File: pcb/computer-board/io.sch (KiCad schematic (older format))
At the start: 17 parts, among them J4 Conn_02x20_Odd_Even, U5 SN74AVC16T245DGGR, U6 SN74AVC4T245PWR, U7 74LVC1G14GW,125

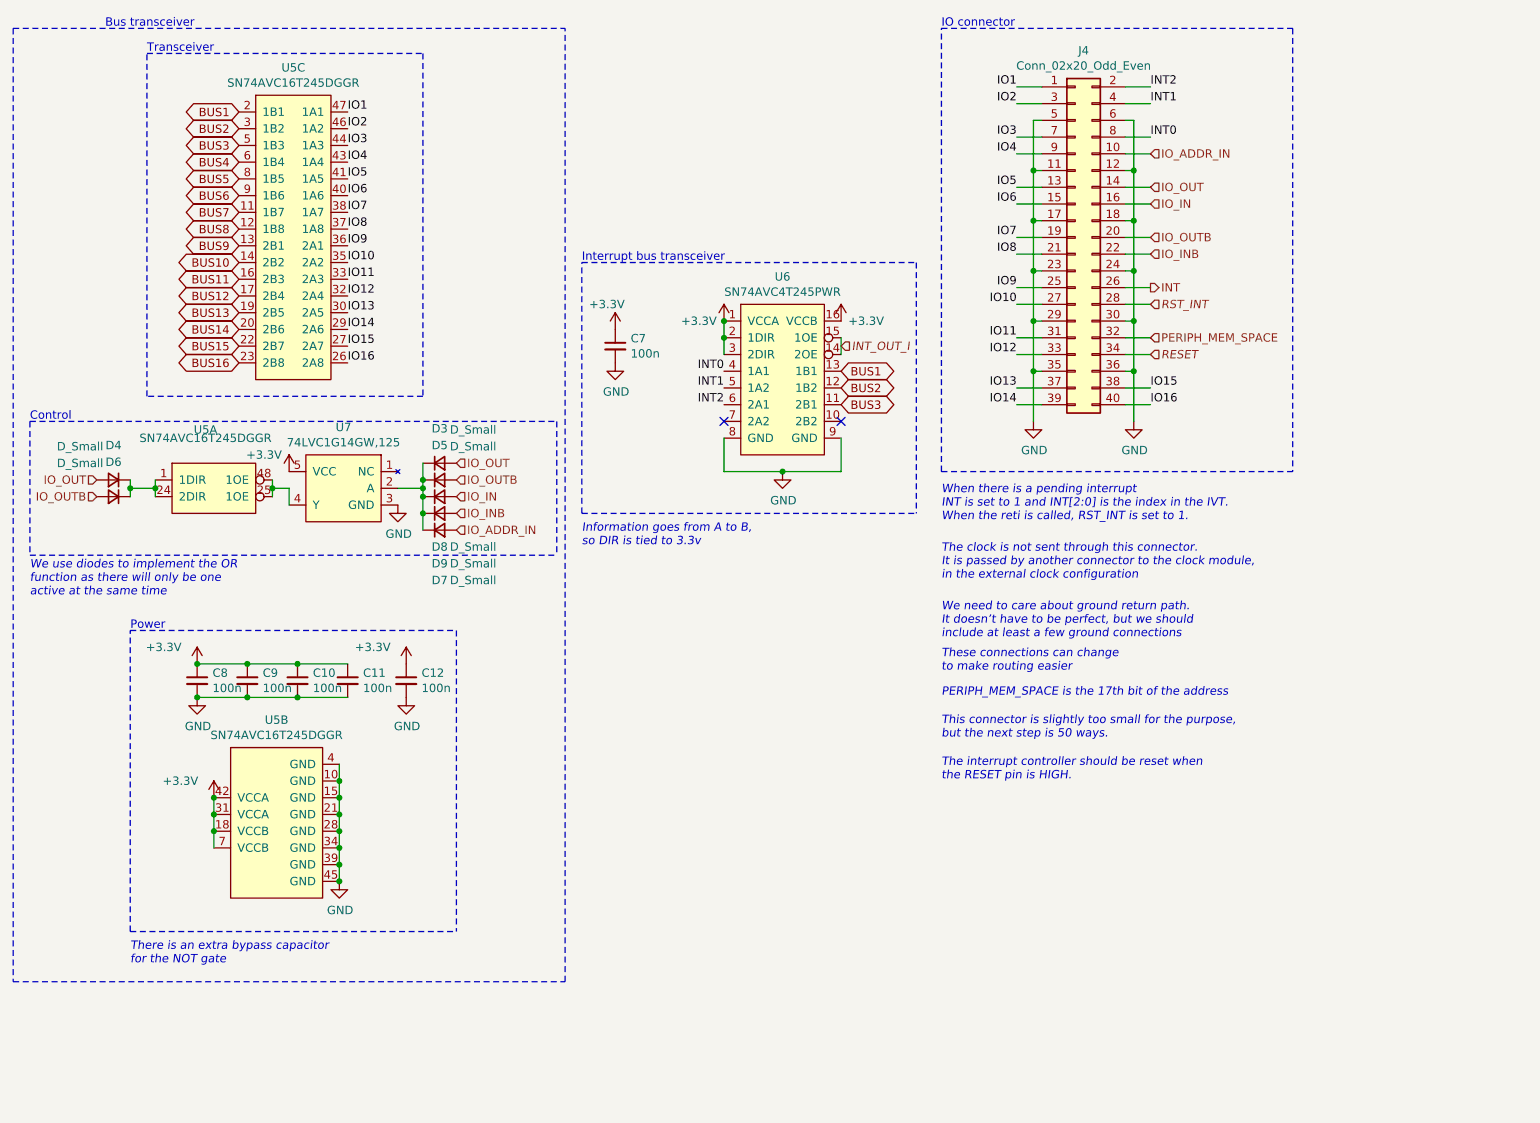
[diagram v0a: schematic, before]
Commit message: Remove and change connectors for a mezzanine one
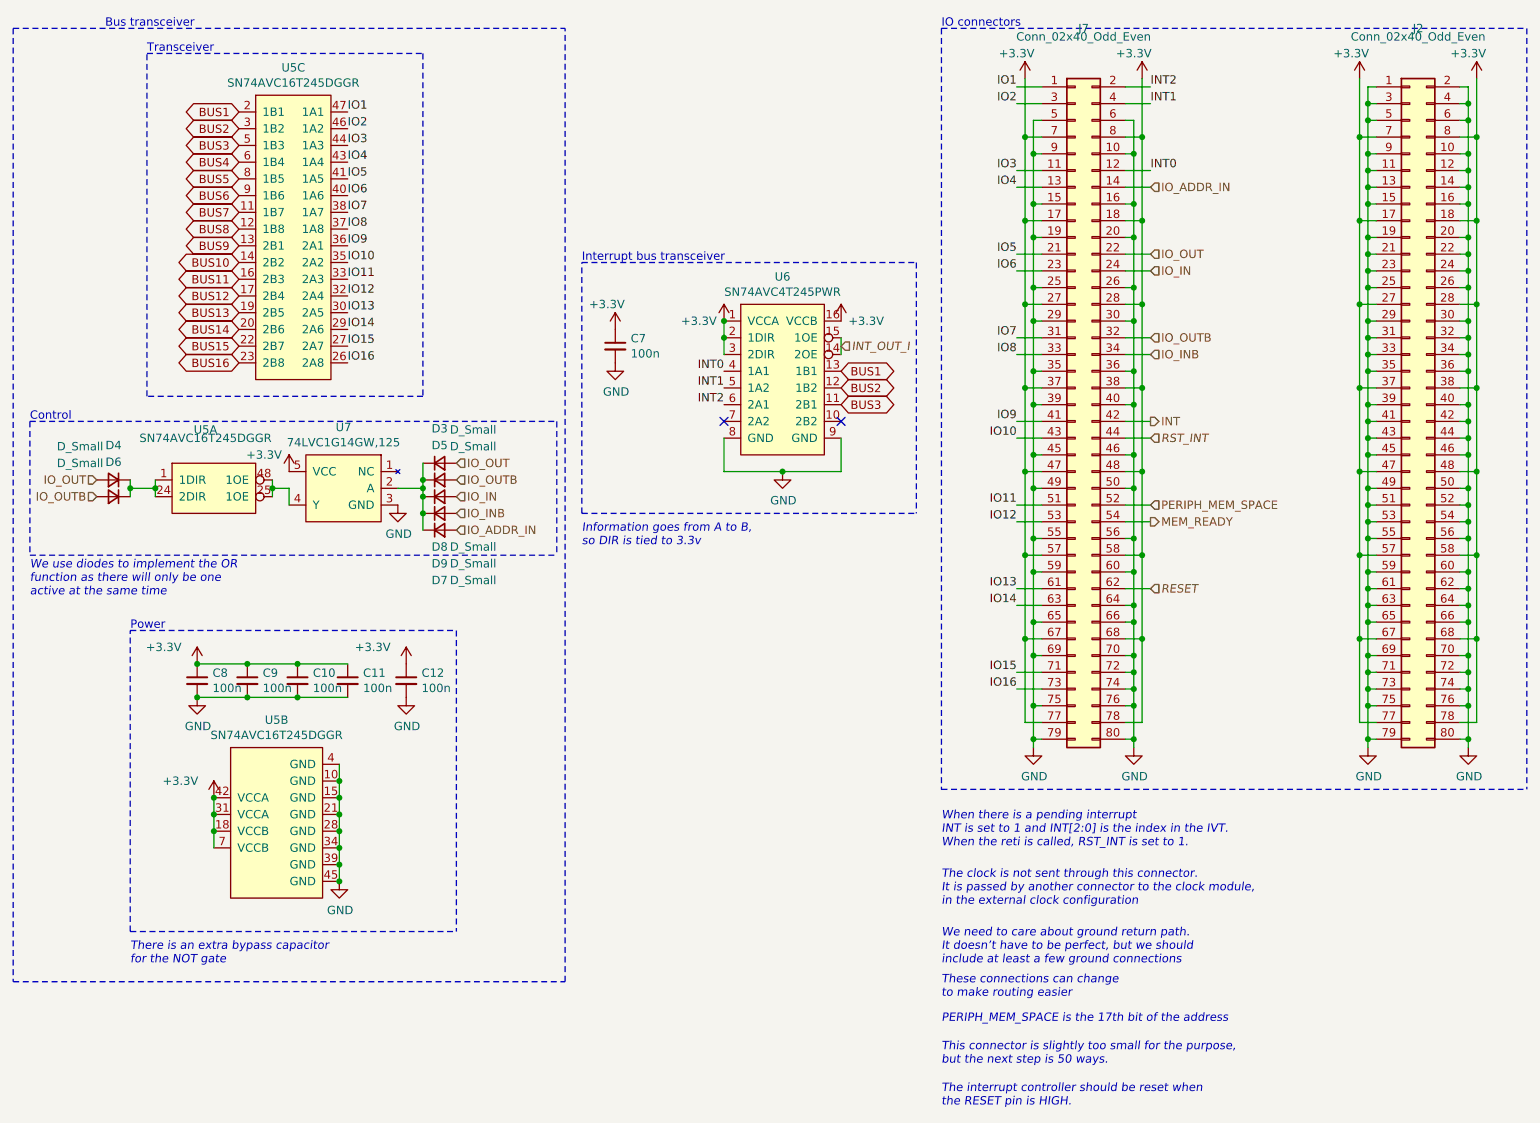
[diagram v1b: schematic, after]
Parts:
- removed J4: Conn_02x20_Odd_Even, Connector_Molex:Micro-Lock-Plus-02x20, symbol Connector_Generic:Conn_02x20_Odd_Even
- added J2, J7: Conn_02x40_Odd_Even, Connector_Hirose:HRS_DF17(2.0)-80DP-0.5V(57), symbol Connector_Generic:Conn_02x40_Odd_Even
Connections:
- net +3V3: now also J2.17 (Pin_17), J2.18 (Pin_18), J2.27 (Pin_27), J2.28 (Pin_28), J2.37 (Pin_37), J2.38 (Pin_38), J2.47 (Pin_47), J2.48 (Pin_48), J2.57 (Pin_57), J2.58 (Pin_58), J2.67 (Pin_67), J2.68 (Pin_68), J2.7 (Pin_7), J2.77 (Pin_77), J2.78 (Pin_78), J2.8 (Pin_8), J7.17 (Pin_17), J7.18 (Pin_18), J7.27 (Pin_27), J7.28 (Pin_28), J7.37 (Pin_37), J7.38 (Pin_38), J7.47 (Pin_47), J7.48 (Pin_48), J7.57 (Pin_57), J7.58 (Pin_58), J7.67 (Pin_67), J7.68 (Pin_68), J7.7 (Pin_7), J7.77 (Pin_77), J7.78 (Pin_78), J7.8 (Pin_8)
- net GND: now also J2.1 (Pin_1), J2.10 (Pin_10), J2.11 (Pin_11), J2.12 (Pin_12), J2.13 (Pin_13), J2.14 (Pin_14), J2.15 (Pin_15), J2.16 (Pin_16), J2.19 (Pin_19), J2.2 (Pin_2), J2.20 (Pin_20), J2.21 (Pin_21), J2.22 (Pin_22), J2.23 (Pin_23), J2.24 (Pin_24), J2.25 (Pin_25), J2.26 (Pin_26), J2.29 (Pin_29), J2.3 (Pin_3), J2.30 (Pin_30), J2.31 (Pin_31), J2.32 (Pin_32), J2.33 (Pin_33), J2.34 (Pin_34), J2.35 (Pin_35), J2.36 (Pin_36), J2.39 (Pin_39), J2.4 (Pin_4), J2.40 (Pin_40), J2.41 (Pin_41), J2.42 (Pin_42), J2.43 (Pin_43), J2.44 (Pin_44), J2.45 (Pin_45), J2.46 (Pin_46), J2.49 (Pin_49), J2.5 (Pin_5), J2.50 (Pin_50), J2.51 (Pin_51), J2.52 (Pin_52), J2.53 (Pin_53), J2.54 (Pin_54), J2.55 (Pin_55), J2.56 (Pin_56), J2.59 (Pin_59), J2.6 (Pin_6), J2.60 (Pin_60), J2.61 (Pin_61), J2.62 (Pin_62), J2.63 (Pin_63), J2.64 (Pin_64), J2.65 (Pin_65), J2.66 (Pin_66), J2.69 (Pin_69), J2.70 (Pin_70), J2.71 (Pin_71), J2.72 (Pin_72), J2.73 (Pin_73), J2.74 (Pin_74), J2.75 (Pin_75), J2.76 (Pin_76), J2.79 (Pin_79), J2.80 (Pin_80), J2.9 (Pin_9), J7.10 (Pin_10), J7.15 (Pin_15), J7.16 (Pin_16), J7.19 (Pin_19), J7.20 (Pin_20), J7.25 (Pin_25), J7.26 (Pin_26), J7.29 (Pin_29), J7.30 (Pin_30), J7.35 (Pin_35), J7.36 (Pin_36), J7.39 (Pin_39), J7.40 (Pin_40), J7.45 (Pin_45), J7.46 (Pin_46), J7.49 (Pin_49), J7.5 (Pin_5), J7.50 (Pin_50), J7.55 (Pin_55), J7.56 (Pin_56), J7.59 (Pin_59), J7.6 (Pin_6), J7.60 (Pin_60), J7.64 (Pin_64), J7.65 (Pin_65), J7.66 (Pin_66), J7.69 (Pin_69), J7.70 (Pin_70), J7.72 (Pin_72), J7.74 (Pin_74), J7.75 (Pin_75), J7.76 (Pin_76), J7.79 (Pin_79), J7.80 (Pin_80), J7.9 (Pin_9)
- net INT: now also J7.42 (Pin_42)
- net INT0: now also J7.12 (Pin_12)
- net INT1: now also J7.4 (Pin_4)
- net INT2: now also J7.2 (Pin_2)
- net IO1: now also J7.1 (Pin_1)
- net IO10: now also J7.43 (Pin_43)
- net IO11: now also J7.51 (Pin_51)
- net IO12: now also J7.53 (Pin_53)
- net IO13: now also J7.61 (Pin_61)
- net IO14: now also J7.63 (Pin_63)
- net IO15: now also J7.71 (Pin_71)
- net IO16: now also J7.73 (Pin_73)
- net IO2: now also J7.3 (Pin_3)
- net IO3: now also J7.11 (Pin_11)
- net IO4: now also J7.13 (Pin_13)
- net IO5: now also J7.21 (Pin_21)
- net IO6: now also J7.23 (Pin_23)
- net IO7: now also J7.31 (Pin_31)
- net IO8: now also J7.33 (Pin_33)
- net IO9: now also J7.41 (Pin_41)
- net IO_ADDR_IN: now also J7.14 (Pin_14)
- net IO_IN: now also J7.24 (Pin_24)
- net IO_INB: now also J7.34 (Pin_34)
- net IO_OUT: now also J7.22 (Pin_22)
- net IO_OUTB: now also J7.32 (Pin_32)
- net PERIPH_MEM_SPACE: now also J7.52 (Pin_52)
- net RESET: now also J7.62 (Pin_62)
- net RST_INT: now also J7.44 (Pin_44)
- new net MEM_READY: J7.54 (Pin_54)
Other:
- note added: "IO connectors"
- note removed: "IO connector"

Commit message: Revision 2 is ready
Need to wait for the testing of rev 1 before ordering
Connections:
- net GND: now also J7.62 (Pin_62); no longer J2.62 (Pin_62), J2.64 (Pin_64), J2.72 (Pin_72), J2.74 (Pin_74)
- net RESET: now also J2.74 (Pin_74); no longer J7.62 (Pin_62)
- new net CLK: J2.64 (Pin_64)
- new net CLK_I: J2.62 (Pin_62)
- new net EXT_CLK: J2.72 (Pin_72)
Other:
- moved on the sheet: J2

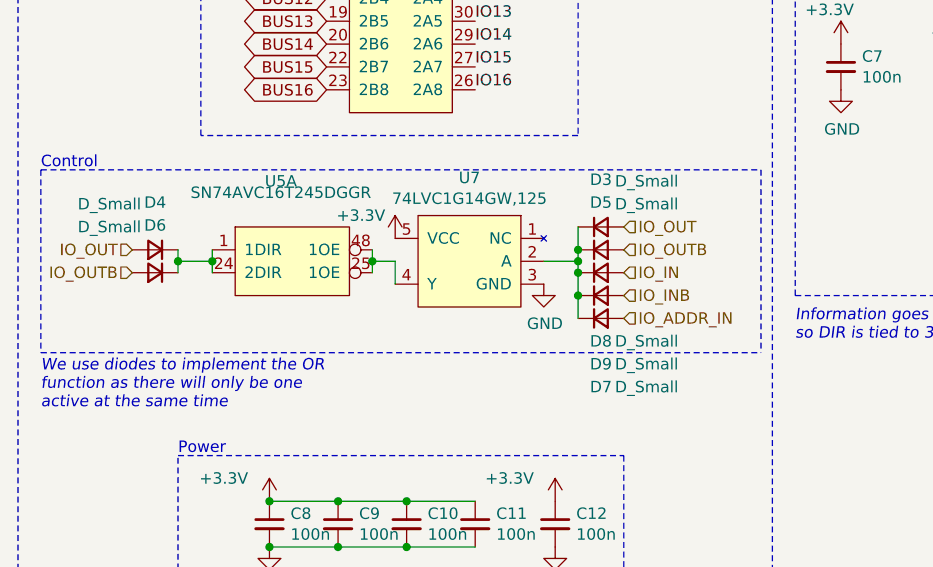
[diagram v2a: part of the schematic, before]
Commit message: added pulldowns on diode logic
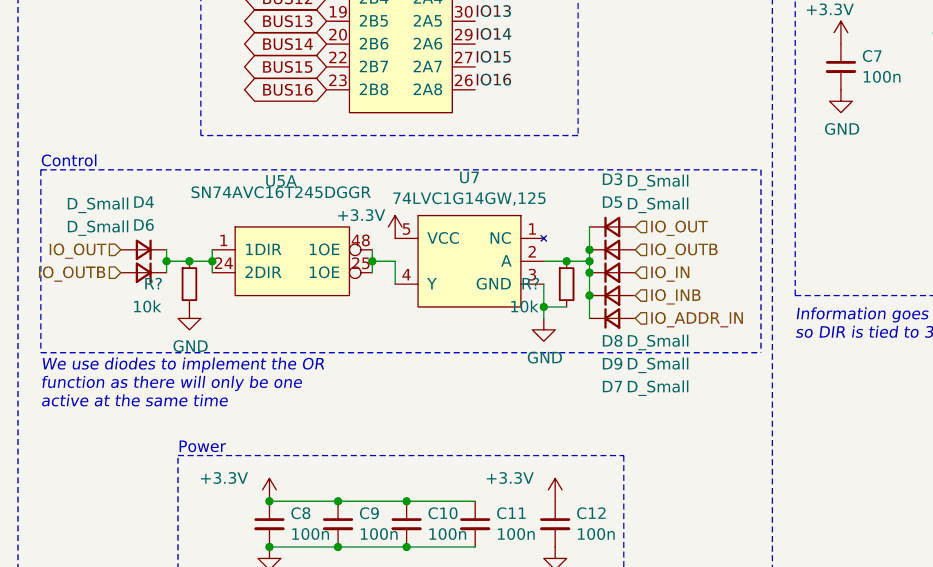
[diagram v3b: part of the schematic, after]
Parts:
- added R? (x2): 10k, Resistor_SMD:R_0402_1005Metric_Pad0.72x0.64mm_HandSolder, symbol Device:R_Small
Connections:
- net GND: now also R?.2, R?.2
- net at D4.1 (K), D6.1 (K), U5.1 (1DIR)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: now also R?.1
- net at D3.1 (K), D5.1 (K), D7.1 (K)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: now also R?.1
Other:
- moved on the sheet: D3, D4, D5, D6, D7, D8, D9
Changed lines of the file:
@@
 Text Notes 1300 750  0    50   ~ 0
 Bus transceiver
-Text HLabel 3400 3350 2    50   Input ~ 0
+Text HLabel 3450 3350 2    50   Input ~ 0
 IO_OUT
-Text HLabel 3400 3450 2    50   Input ~ 0
+Text HLabel 3450 3450 2    50   Input ~ 0
 IO_OUTB
-Text HLabel 3400 3550 2    50   Input ~ 0
+Text HLabel 3450 3550 2    50   Input ~ 0
 IO_IN
-Text HLabel 3400 3650 2    50   Input ~ 0
+Text HLabel 3450 3650 2    50   Input ~ 0
 IO_INB
 $Comp
 L Device:D_Small D?
 U 1 1 5F9B5E06
-P 3300 3350
+P 3350 3350
 AR Path="/5F95DC76/5F9B5E06" Ref="D?"  Part="1"
 AR Path="/5F8B5DB4/5F9B5E06" Ref="D3"  Part="1"
-F 0 "D3" H 3300 3557 50  0000 C CNN
-F 1 "D_Small" H 3500 3550 50  0000 C CNN
-F 2 "Diode_SMD:D_0603_1608Metric_Pad1.05x0.95mm_HandSolder" V 3300 3350 50  0001 C CNN
-F 3 "~" V 3300 3350 50  0001 C CNN
-	1    3300 3350
+F 0 "D3" H 3350 3557 50  0000 C CNN
+F 1 "D_Small" H 3550 3550 50  0000 C CNN
+F 2 "Diode_SMD:D_0603_1608Metric_Pad1.05x0.95mm_HandSolder" V 3350 3350 50  0001 C CNN
+F 3 "~" V 3350 3350 50  0001 C CNN
+	1    3350 3350
 	1    0    0    -1
 $EndComp
@@
 L Device:D_Small D?
 U 1 1 5F9B5E0C
-P 3300 3450
+P 3350 3450
 AR Path="/5F95DC76/5F9B5E0C" Ref="D?"  Part="1"
 AR Path="/5F8B5DB4/5F9B5E0C" Ref="D5"  Part="1"
-F 0 "D5" H 3300 3657 50  0000 C CNN
-F 1 "D_Small" H 3500 3650 50  0000 C CNN
-F 2 "Diode_SMD:D_0603_1608Metric_Pad1.05x0.95mm_HandSolder" V 3300 3450 50  0001 C CNN
-F 3 "~" V 3300 3450 50  0001 C CNN
-	1    3300 3450
+F 0 "D5" H 3350 3657 50  0000 C CNN
+F 1 "D_Small" H 3550 3650 50  0000 C CNN
+F 2 "Diode_SMD:D_0603_1608Metric_Pad1.05x0.95mm_HandSolder" V 3350 3450 50  0001 C CNN
+F 3 "~" V 3350 3450 50  0001 C CNN
+	1    3350 3450
 	1    0    0    -1
 $EndComp
@@
 L Device:D_Small D?
 U 1 1 5F9B5E12
-P 3300 3550
+P 3350 3550
 AR Path="/5F95DC76/5F9B5E12" Ref="D?"  Part="1"
 AR Path="/5F8B5DB4/5F9B5E12" Ref="D7"  Part="1"
-F 0 "D7" H 3300 3050 50  0000 C CNN
-F 1 "D_Small" H 3500 3050 50  0000 C CNN
-F 2 "Diode_SMD:D_0603_1608Metric_Pad1.05x0.95mm_HandSolder" V 3300 3550 50  0001 C CNN
-F 3 "~" V 3300 3550 50  0001 C CNN
-	1    3300 3550
+F 0 "D7" H 3350 3050 50  0000 C CNN
+F 1 "D_Small" H 3550 3050 50  0000 C CNN
+F 2 "Diode_SMD:D_0603_1608Metric_Pad1.05x0.95mm_HandSolder" V 3350 3550 50  0001 C CNN
+F 3 "~" V 3350 3550 50  0001 C CNN
+	1    3350 3550
 	1    0    0    -1
 $EndComp
@@
 L Device:D_Small D?
 U 1 1 5F9B5E18
-P 3300 3650
+P 3350 3650
 AR Path="/5F95DC76/5F9B5E18" Ref="D?"  Part="1"
 AR Path="/5F8B5DB4/5F9B5E18" Ref="D8"  Part="1"
-F 0 "D8" H 3300 3450 50  0000 C CNN
-F 1 "D_Small" H 3500 3450 50  0000 C CNN
-F 2 "Diode_SMD:D_0603_1608Metric_Pad1.05x0.95mm_HandSolder" V 3300 3650 50  0001 C CNN
-F 3 "~" V 3300 3650 50  0001 C CNN
-	1    3300 3650
-	1    0    0    -1
-$EndComp
-Connection ~ 3200 3450
-Connection ~ 3200 3550
-Wire Wire Line
-	3200 3550 3200 3650
+F 0 "D8" H 3350 3450 50  0000 C CNN
+F 1 "D_Small" H 3550 3450 50  0000 C CNN
+F 2 "Diode_SMD:D_0603_1608Metric_Pad1.05x0.95mm_HandSolder" V 3350 3650 50  0001 C CNN
+F 3 "~" V 3350 3650 50  0001 C CNN
+	1    3350 3650
+	1    0    0    -1
+$EndComp
+Connection ~ 3250 3450
+Connection ~ 3250 3550
+Wire Wire Line
+	3250 3550 3250 3650
 $Comp
 L Device:D_Small D?
 U 1 1 5F9B5E22
-P 3300 3750
+P 3350 3750
 AR Path="/5F95DC76/5F9B5E22" Ref="D?"  Part="1"
 AR Path="/5F8B5DB4/5F9B5E22" Ref="D9"  Part="1"
-F 0 "D9" H 3300 3550 50  0000 C CNN
-F 1 "D_Small" H 3500 3550 50  0000 C CNN
-F 2 "Diode_SMD:D_0603_1608Metric_Pad1.05x0.95mm_HandSolder" V 3300 3750 50  0001 C CNN
-F 3 "~" V 3300 3750 50  0001 C CNN
-	1    3300 3750
-	1    0    0    -1
-$EndComp
-Wire Wire Line
-	3200 3750 3200 3650
-Connection ~ 3200 3650
-Text HLabel 3400 3750 2    50   Input ~ 0
+F 0 "D9" H 3350 3550 50  0000 C CNN
+F 1 "D_Small" H 3550 3550 50  0000 C CNN
+F 2 "Diode_SMD:D_0603_1608Metric_Pad1.05x0.95mm_HandSolder" V 3350 3750 50  0001 C CNN
+F 3 "~" V 3350 3750 50  0001 C CNN
+	1    3350 3750
+	1    0    0    -1
+$EndComp
+Wire Wire Line
+	3250 3750 3250 3650
+Connection ~ 3250 3650
+Text HLabel 3450 3750 2    50   Input ~ 0
 IO_ADDR_IN
 Wire Wire Line
-	3200 3450 3200 3500
+	3250 3450 3250 3500
 Wire Wire Line
 	2300 3450 2300 3500
 Wire Wire Line
-	3200 3350 3200 3450
-Wire Wire Line
-	3200 3500 3050 3500
-Connection ~ 3200 3500
-Wire Wire Line
-	3200 3500 3200 3550
+	3250 3350 3250 3450
+Wire Wire Line
+	3250 3500 3150 3500
+Connection ~ 3250 3500
+Wire Wire Line
+	3250 3500 3250 3550
 Wire Wire Line
 	2400 3600 2400 3500
@@
 L power:GND #PWR?
 U 1 1 5F9B5E41
-P 3050 3600
+P 3050 3750
 AR Path="/5F95DC76/5F9B5E41" Ref="#PWR?"  Part="1"
 AR Path="/5F8B5DB4/5F9B5E41" Ref="#PWR0135"  Part="1"
-F 0 "#PWR0135" H 3050 3350 50  0001 C CNN
-F 1 "GND" H 3055 3427 50  0000 C CNN
-F 2 "" H 3050 3600 50  0001 C CNN
-F 3 "" H 3050 3600 50  0001 C CNN
-	1    3050 3600
+F 0 "#PWR0135" H 3050 3500 50  0001 C CNN
+F 1 "GND" H 3055 3577 50  0000 C CNN
+F 2 "" H 3050 3750 50  0001 C CNN
+F 3 "" H 3050 3750 50  0001 C CNN
+	1    3050 3750
 	1    0    0    -1
 $EndComp
@@
 Text Notes 850  4150 0    50   Italic 0
 We use diodes to implement the OR\nfunction as there will only be one \nactive at the same time
-Text HLabel 1250 3450 0    50   Input ~ 0
+Text HLabel 1200 3450 0    50   Input ~ 0
 IO_OUT
-Text HLabel 1250 3550 0    50   Input ~ 0
+Text HLabel 1200 3550 0    50   Input ~ 0
 IO_OUTB
 $Comp
 L Device:D_Small D?
 U 1 1 5F9E6C34
-P 1350 3450
+P 1300 3450
 AR Path="/5F95DC76/5F9E6C34" Ref="D?"  Part="1"
 AR Path="/5F8B5DB4/5F9E6C34" Ref="D4"  Part="1"
-F 0 "D4" H 1350 3657 50  0000 C CNN
-F 1 "D_Small" H 1550 3650 50  0000 C CNN
-F 2 "Diode_SMD:D_0603_1608Metric_Pad1.05x0.95mm_HandSolder" V 1350 3450 50  0001 C CNN
-F 3 "~" V 1350 3450 50  0001 C CNN
-	1    1350 3450
+F 0 "D4" H 1300 3657 50  0000 C CNN
+F 1 "D_Small" H 1500 3650 50  0000 C CNN
+F 2 "Diode_SMD:D_0603_1608Metric_Pad1.05x0.95mm_HandSolder" V 1300 3450 50  0001 C CNN
+F 3 "~" V 1300 3450 50  0001 C CNN
+	1    1300 3450
 	-1   0    0    -1
 $EndComp
@@
 L Device:D_Small D?
 U 1 1 5F9E6C3A
-P 1350 3550
+P 1300 3550
 AR Path="/5F95DC76/5F9E6C3A" Ref="D?"  Part="1"
 AR Path="/5F8B5DB4/5F9E6C3A" Ref="D6"  Part="1"
-F 0 "D6" H 1350 3757 50  0000 C CNN
-F 1 "D_Small" H 1550 3750 50  0000 C CNN
-F 2 "Diode_SMD:D_0603_1608Metric_Pad1.05x0.95mm_HandSolder" V 1350 3550 50  0001 C CNN
-F 3 "~" V 1350 3550 50  0001 C CNN
-	1    1350 3550
+F 0 "D6" H 1300 3757 50  0000 C CNN
+F 1 "D_Small" H 1500 3750 50  0000 C CNN
+F 2 "Diode_SMD:D_0603_1608Metric_Pad1.05x0.95mm_HandSolder" V 1300 3550 50  0001 C CNN
+F 3 "~" V 1300 3550 50  0001 C CNN
+	1    1300 3550
 	-1   0    0    -1
 $EndComp
 Wire Wire Line
-	1450 3450 1450 3500
-Wire Wire Line
 	1600 3450 1600 3500
-Wire Wire Line
-	1450 3500 1600 3500
-Connection ~ 1450 3500
-Wire Wire Line
-	1450 3500 1450 3550
 Connection ~ 1600 3500
 Wire Wire Line
@@
 Wire Wire Line
 	9200 4500 9200 4800
+$Comp
+L Device:R_Small R?
+U 1 1 60033A38
+P 1500 3600
+AR Path="/60033A38" Ref="R?"  Part="1"
+AR Path="/5F8B5DB4/60033A38" Ref="R?"  Part="1"
+F 0 "R?" H 1300 3600 50  0000 L CNN
+F 1 "10k" H 1250 3500 50  0000 L CNN
+F 2 "Resistor_SMD:R_0402_1005Metric_Pad0.72x0.64mm_HandSolder" H 1500 3600 50  0001 C CNN
+F 3 "~" H 1500 3600 50  0001 C CNN
+	1    1500 3600
+	1    0    0    -1
+$EndComp
+$Comp
+L Device:R_Small R?
+U 1 1 6004A131
+P 3150 3600
+AR Path="/6004A131" Ref="R?"  Part="1"
+AR Path="/5F8B5DB4/6004A131" Ref="R?"  Part="1"
+F 0 "R?" H 2950 3600 50  0000 L CNN
+F 1 "10k" H 2900 3500 50  0000 L CNN
+F 2 "Resistor_SMD:R_0402_1005Metric_Pad0.72x0.64mm_HandSolder" H 3150 3600 50  0001 C CNN
+F 3 "~" H 3150 3600 50  0001 C CNN
+	1    3150 3600
+	1    0    0    -1
+$EndComp
+Wire Wire Line
+	3050 3600 3050 3700
+Connection ~ 3050 3700
+Wire Wire Line
+	3050 3700 3050 3750
+Wire Wire Line
+	3050 3500 3150 3500
+Connection ~ 3150 3500
+Wire Wire Line
+	3050 3700 3150 3700
+Connection ~ 1500 3500
+Wire Wire Line
+	1500 3500 1600 3500
+Wire Wire Line
+	1400 3500 1400 3450
+Wire Wire Line
+	1400 3500 1500 3500
+Wire Wire Line
+	1400 3550 1400 3500
+Connection ~ 1400 3500
+$Comp
+L power:GND #PWR?
+U 1 1 6010C509
+P 1500 3700
+AR Path="/5F95DC76/6010C509" Ref="#PWR?"  Part="1"
+AR Path="/5F8B5DB4/6010C509" Ref="#PWR?"  Part="1"
+F 0 "#PWR?" H 1500 3450 50  0001 C CNN
+F 1 "GND" H 1505 3527 50  0000 C CNN
+F 2 "" H 1500 3700 50  0001 C CNN
+F 3 "" H 1500 3700 50  0001 C CNN
+	1    1500 3700
+	1    0    0    -1
+$EndComp
 $EndSCHEMATC
